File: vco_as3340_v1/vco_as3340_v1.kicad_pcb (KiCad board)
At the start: 2 copper layers, 40 x 100 mm, 88 parts, among them J1 Conn_02x05_Odd_Even, J2 FREQ_CV, J3 SOFT_SYNC, J4 TRIANGLE, J5 SAWTOOTH, J6 PULSE, U1 LM7805_TO220, U2 L7905, U3 AS3340, U4 TL072, U5 TL072, U6 TL072, U7 TL072

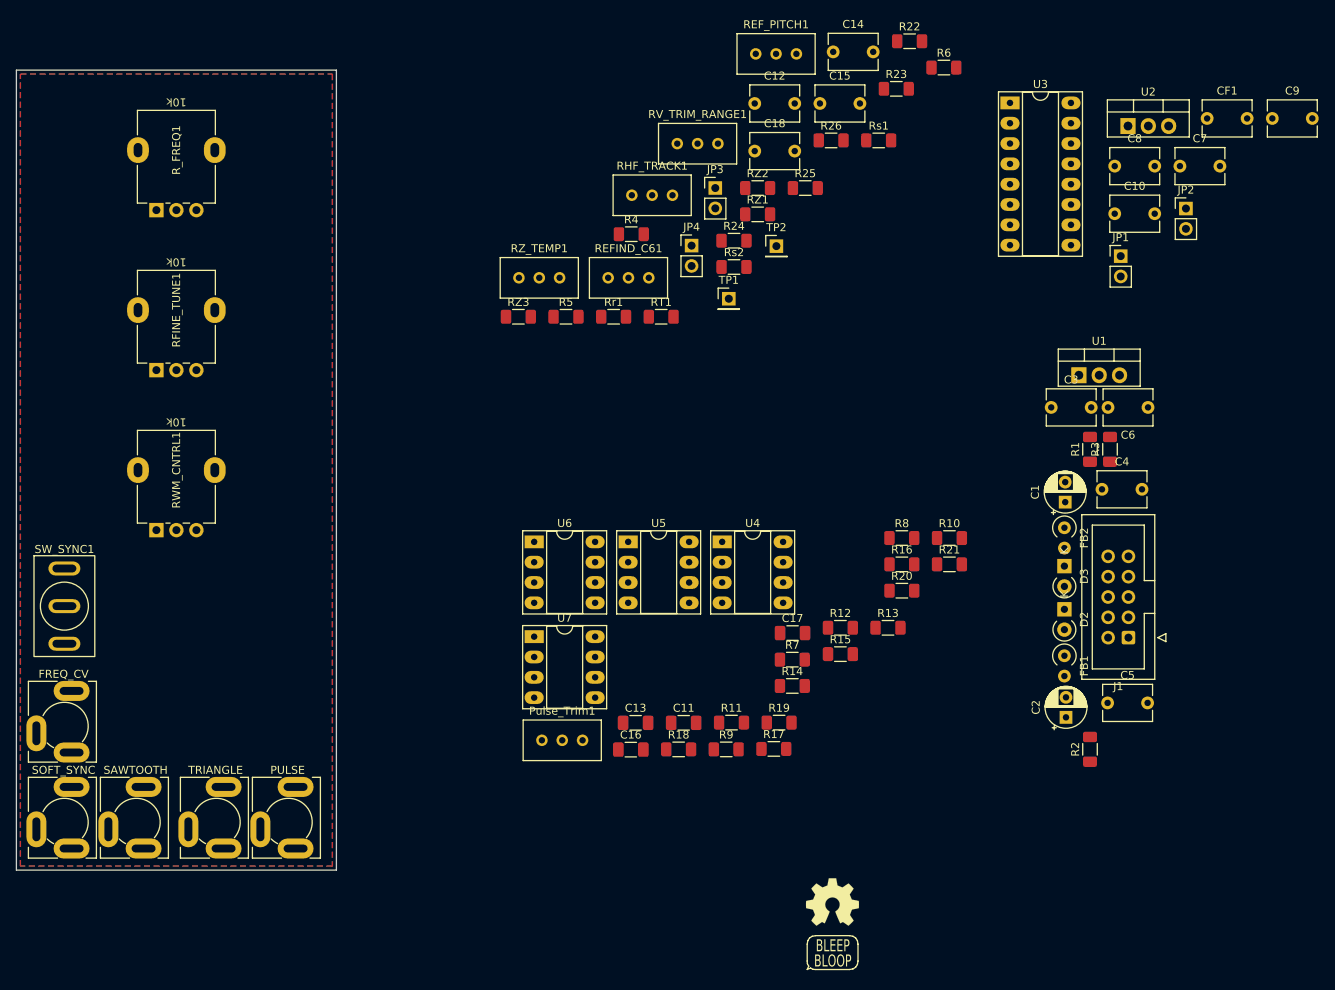
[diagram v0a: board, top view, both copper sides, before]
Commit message: Schematic update from breadboarding, start layout
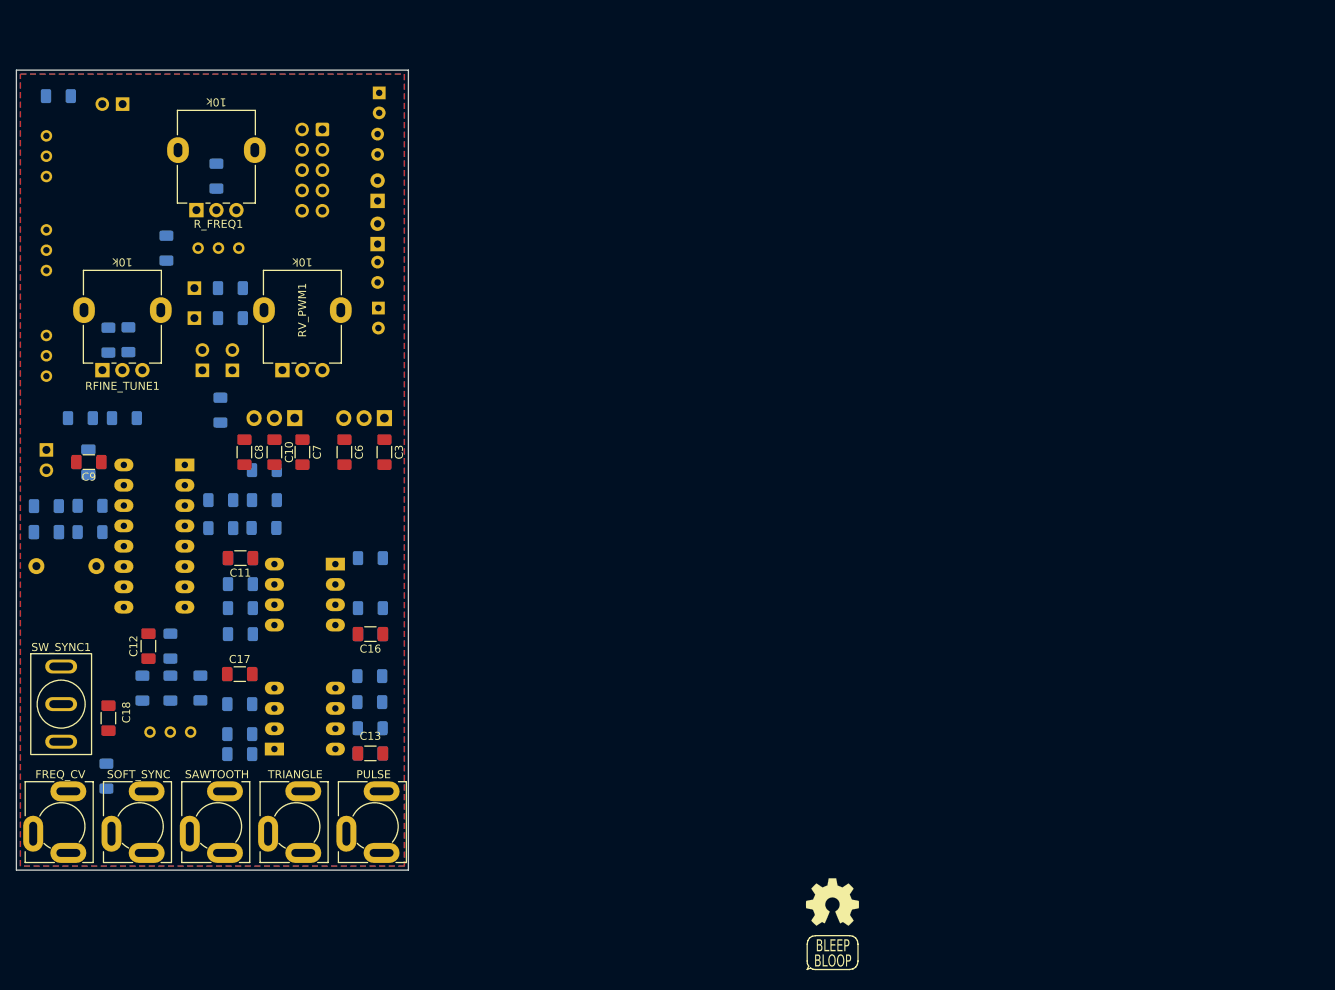
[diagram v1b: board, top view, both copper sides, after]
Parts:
- removed C4, C5: 10nF, Capacitor_THT:C_Disc_D6.0mm_W4.4mm_P5.00mm
- removed Pulse_Trim1: 100k, Potentiometer_THT:Potentiometer_Bourns_3296W_Vertical
- removed RV_TRIM_RANGE1: 1k, Potentiometer_THT:Potentiometer_Bourns_3296W_Vertical
- removed RWM_CNTRL1: 10k, My Stuff:Potentiometer_Alpha_RD901F-40-00D_Single_Vertical_w_3d
- removed RZ3: 18k, Resistor_SMD:R_1206_3216Metric_Pad1.30x1.75mm_HandSolder
- removed U6, U7: TL072, Package_DIP:DIP-8_W7.62mm_Socket_LongPads
- added R27: 15k, Resistor_SMD:R_1206_3216Metric_Pad1.30x1.75mm_HandSolder, B.Cu at (184.2, 111.0)
- added R28: 15k, Resistor_SMD:R_1206_3216Metric_Pad1.30x1.75mm_HandSolder, B.Cu at (168.0, 111.0)
- added R29: 100k, Resistor_SMD:R_1206_3216Metric_Pad1.30x1.75mm_HandSolder, B.Cu at (167.9, 129.2)
- added R30: 100k, Resistor_SMD:R_1206_3216Metric_Pad1.30x1.75mm_HandSolder, B.Cu at (167.9, 133.0)
- added RV_PWM1: 10k, My Stuff:Potentiometer_Alpha_RD901F-40-00D_Single_Vertical_w_3d, F.Cu at (175.8, 80.0)
- added RV_SCALE_ADJ1: 1k, Potentiometer_THT:Potentiometer_Bourns_3296W_Vertical, B.Cu at (143.8, 75.0)
- added Rr2: 330k, Resistor_SMD:R_1206_3216Metric_Pad1.30x1.75mm_HandSolder, B.Cu at (153.5, 93.5)
- C1, C2, D2, D3, FB1, FB2, J1, JP1, JP2, JP3, JP4, R1, R11, R12, R13, R14, R15, R16, R17, R18, R19, R20, R21, R23, R24, R25, R26, R3, R4, R5, R6, R7, R8, REFIND_C61, REF_PITCH1, RHF_TRACK1, RT1, RZ1, RZ_TEMP1, TP1, TP2, U1, U2, U3, U4, U5: moved to B.Cu
- C10, C12, C18, C3, C6, C7, C8, C9: footprint Capacitor_THT:C_Disc_D6.0mm_W4.4mm_P5.00mm -> Capacitor_SMD:C_1206_3216Metric_Pad1.33x1.80mm_HandSolder
- C14, C15: footprint Capacitor_THT:C_Disc_D6.0mm_W4.4mm_P5.00mm -> Capacitor_SMD:C_1206_3216Metric_Pad1.33x1.80mm_HandSolder; moved to B.Cu
- CF1: footprint Capacitor_THT:C_Disc_D6.0mm_W4.4mm_P5.00mm -> Capacitor_THT:C_Rect_L10.0mm_W2.5mm_P7.50mm_MKS4; moved to B.Cu
- R10: value 100k -> 200k; moved to B.Cu
- R2: value 220k -> 150k; moved to B.Cu
- R22: value 470 -> 1M; moved to B.Cu
- R9: value 100k -> 120k; moved to B.Cu
- RZ2: value 18k -> 13k; moved to B.Cu
- Rr1: value 1.8M -> 1M; moved to B.Cu
- Rs1: value 1.62k -> 1k; moved to B.Cu
- Rs2: value 1.5k -> 620; moved to B.Cu
- moved C9 154.0 mm to (149.1, 99.0), turned to 180 degrees
- moved R2 152.6 mm to (145.2, 53.2), turned to 0 degrees
- moved CF1 149.7 mm to (150.0, 112.0), turned to 180 degrees
- moved R3 131.9 mm to (151.2, 138.2), turned to -90 degrees
- moved R22 122.8 mm to (159.2, 127.2), turned to -90 degrees
- moved JP2 120.9 mm to (167.0, 87.5)
- moved J1 119.1 mm to (178.3, 57.4)
- moved C2 116.0 mm to (185.4, 52.8), turned to -90 degrees
- moved JP1 115.7 mm to (163.2, 87.5)
- moved C7 115.4 mm to (175.8, 97.8), turned to -90 degrees
- moved C14 115.2 mm to (143.8, 107.8), turned to 180 degrees
- moved C8 114.5 mm to (168.5, 97.8), turned to -90 degrees
- moved U3 112.6 mm to (161.1, 99.3), turned to 180 degrees
- moved U2 110.4 mm to (174.8, 93.5), turned to 180 degrees
- moved R6 109.9 mm to (151.5, 83.8), turned to 90 degrees
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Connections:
- C15 pad 1: Net-(RV_TRIM_RANGE1-Pad2) -> GND
- J2 pad R: (no net) -> unconnected-(J2-PadR)
- J3 pad R: (no net) -> unconnected-(J3-PadR)
- J4 pad R: (no net) -> unconnected-(J4-PadR)
- J5 pad R: (no net) -> unconnected-(J5-PadR)
- J6 pad R: (no net) -> unconnected-(J6-PadR)
- R14 pad 1: Net-(R13-Pad2) -> Net-(R14-Pad1)
- R15 pad 2: Net-(R11-Pad1) -> Net-(R15-Pad2)
- RZ2 pad 1: Net-(RZ2-Pad1) -> /Inputs/Scale Adjust 1
- Rr1 pad 1: /Inputs/Linear FM -> Net-(Rr1-Pad1)
- Rs1 pad 2: Net-(RV_TRIM_RANGE1-Pad1) -> Net-(Rs1-Pad2)
- Rs2 pad 1: Net-(RV_TRIM_RANGE1-Pad3) -> Net-(Rs1-Pad2)
- Rs2 pad 2: GND -> Net-(RV_SCALE_ADJ1-Pad1)
- U4 pad 1: Net-(R13-Pad2) -> Net-(R14-Pad1)
- U4 pad 4: (no net) -> -12V
- U4 pad 5: /Outputs/Triangle Output -> GND
- U4 pad 6: Net-(R10-Pad1) -> Net-(R14-Pad2)
- U4 pad 7: Net-(R10-Pad2) -> Net-(R11-Pad1)
- U4 pad 8: (no net) -> +12V
- U5 pad 4: (no net) -> -12V
- U5 pad 5: GND -> /Outputs/Triangle Output
- U5 pad 6: Net-(R14-Pad2) -> Net-(R10-Pad1)
- U5 pad 7: Net-(R11-Pad1) -> Net-(R10-Pad2)
- U5 pad 8: (no net) -> +12V
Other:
- board size 40 x 100 mm -> 49 x 100 mm
- board text added: "50.8mm = 10HP"
- board text removed: "15.24 = 3HP"

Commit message: Layout and routing done
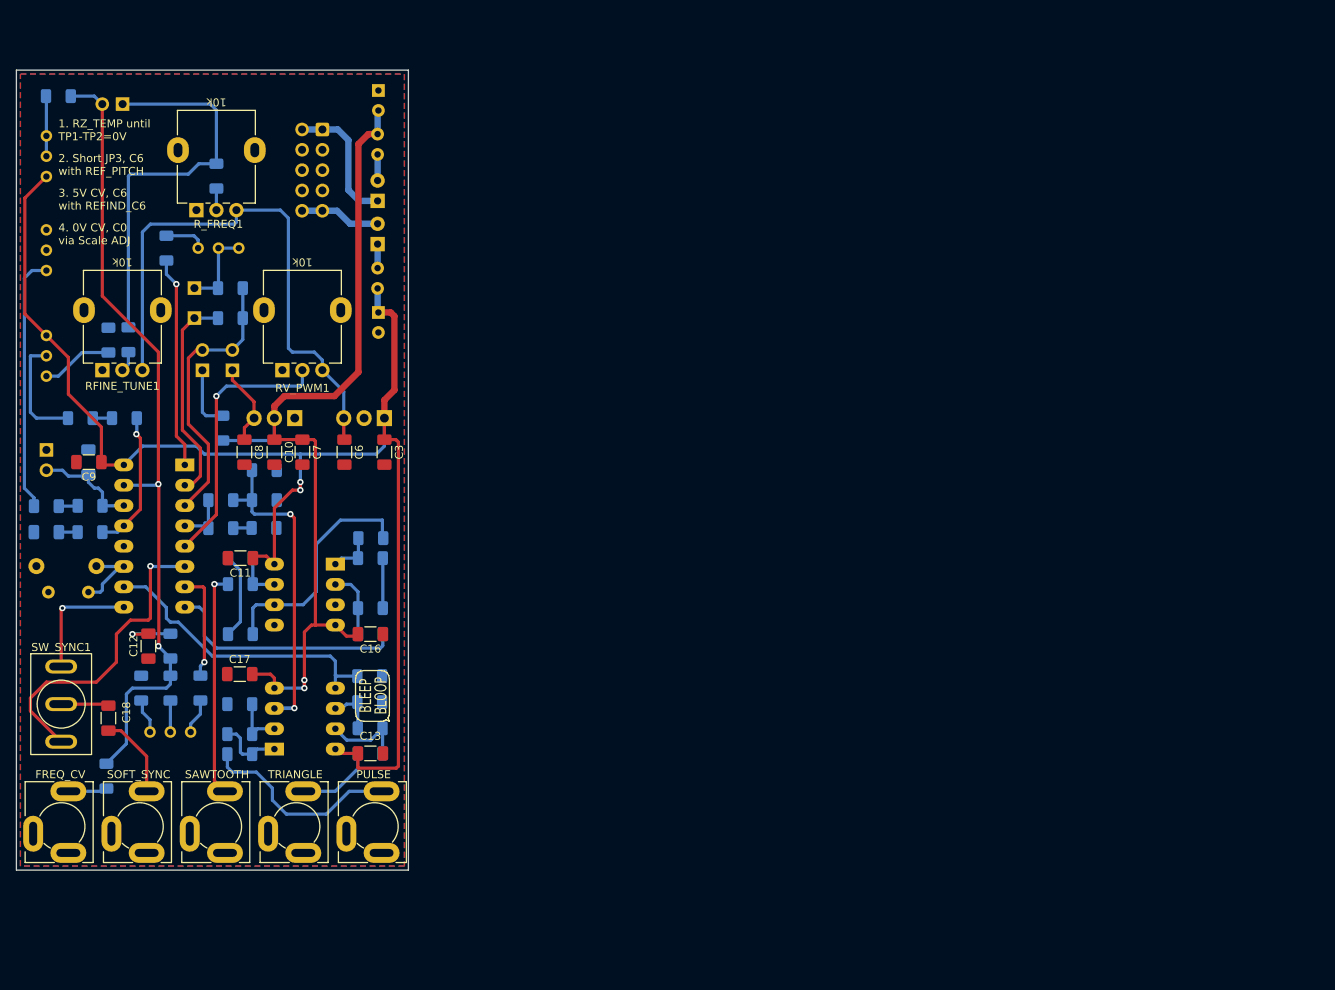
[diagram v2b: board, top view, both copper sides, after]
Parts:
- added CF2: 1nF, Capacitor_THT:C_Rect_L7.0mm_W2.5mm_P5.00mm, B.Cu at (149.0, 115.2)
- LOGO3: moved to B.Cu
- moved LOGO2 98.3 mm to (151.2, 122.8), turned to 90 degrees
- moved LOGO3 78.1 mm to (184.0, 101.8), turned to 180 degrees
- moved LOGO1 65.8 mm to (184.5, 128.2), turned to 90 degrees
- moved R14 18.5 mm to (184.3, 108.5)
- moved R1 2.26 mm to (165.8, 94.8)
- moved FB2 1.79 mm to (185.2, 74.8), turned to -90 degrees
- moved C1 0.55 mm to (185.2, 80.3)
- moved C2 0.32 mm to (185.2, 52.5)
- moved R24 0.15 mm to (155.6, 127.2)
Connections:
- RFINE_TUNE1 pad MP: (no net) -> GND
- RV_PWM1 pad MP: (no net) -> GND
- R_FREQ1 pad MP: (no net) -> GND
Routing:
- net +12V: track 0.00 -> 175.1 mm, vias 0 -> 2
- net -12V: track 0.00 -> 111.7 mm, vias 0 -> 2
- net /Inputs/Frequency Control: track 0.00 -> 100.5 mm, vias 0 -> 2
- net +5V: track 0.00 -> 70.1 mm
- net Net-(JP4-Pad1): track 0.00 -> 49.3 mm
- net Net-(R16-Pad1): track 0.00 -> 41.7 mm, vias 0 -> 2
- net /Inputs/Hard Sync: track 0.00 -> 39.1 mm, vias 0 -> 1
- net /Outputs/Triangle Output: track 0.00 -> 37.2 mm
- net VEE: track 0.00 -> 34.9 mm
- net /Inputs/PWM Control: track 0.00 -> 33.5 mm, vias 0 -> 1
- net Net-(RV_SCALE_ADJ1-Pad1): track 0.00 -> 32.1 mm
- net /Outputs/Sawtooth Output: track 0.00 -> 30.2 mm
- net Net-(R14-Pad2): track 0.00 -> 29.8 mm
- net Net-(J5-PadT): track 0.00 -> 28.1 mm, vias 0 -> 1
- net /Inputs/Scale Adjust 2: track 0.00 -> 26.7 mm
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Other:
- board text added: "1. RZ_TEMP until TP1-TP2=0V"
- board text added: "100k"
- board text added: "10k"
- board text added: "1k"
- board text added: "2. Short JP3, C6 with REF_PITCH"
- board text added: "3. 5V CV, C6 with REFIND_C6"
- board text added: "4. 0V CV, C0 via Scale ADJ"
- board text added: "AS3340"
- board text added: "AS3340 VCO"
- board text added: "LM7805"
- board text added: "LM7905"
- board text added: "RobotDialogs"
- board text added: "TL072"
- board text added: "v1.0 July 2022"

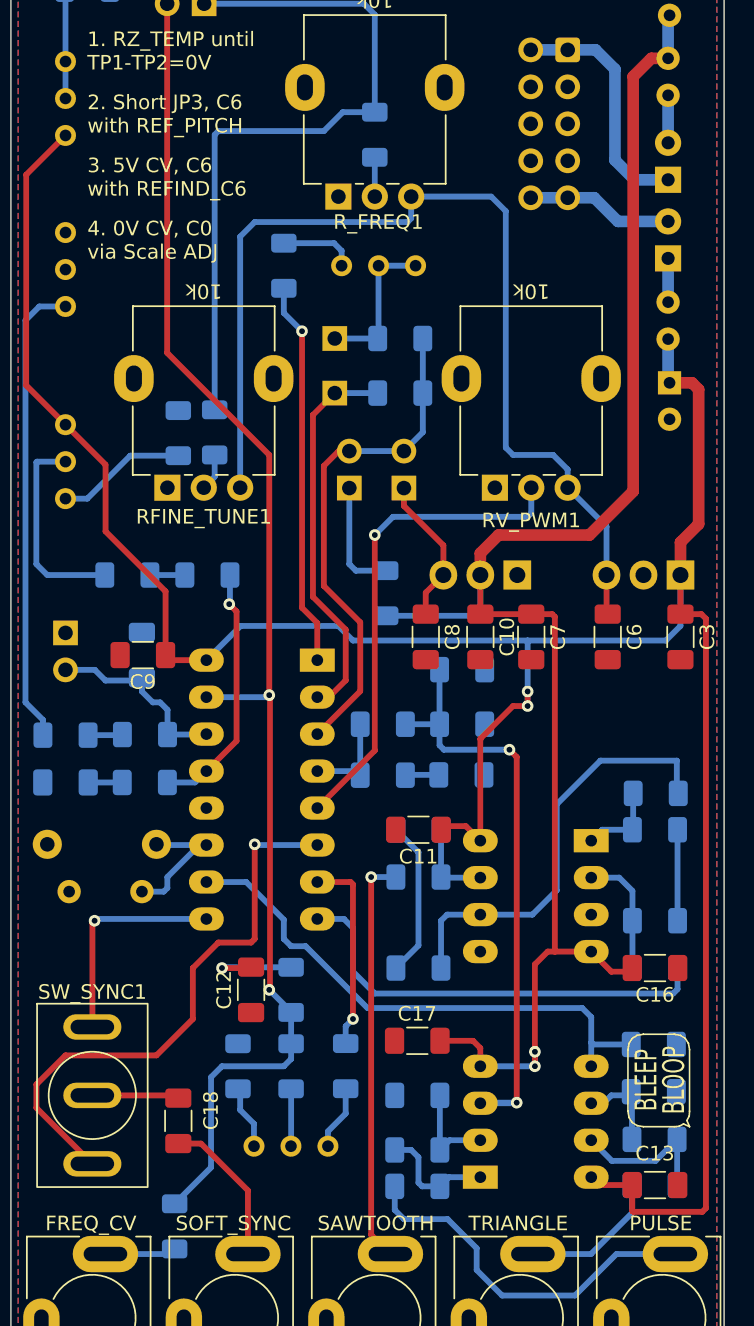
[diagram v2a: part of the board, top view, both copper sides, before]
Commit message: Geographic re-annotate and cleanup
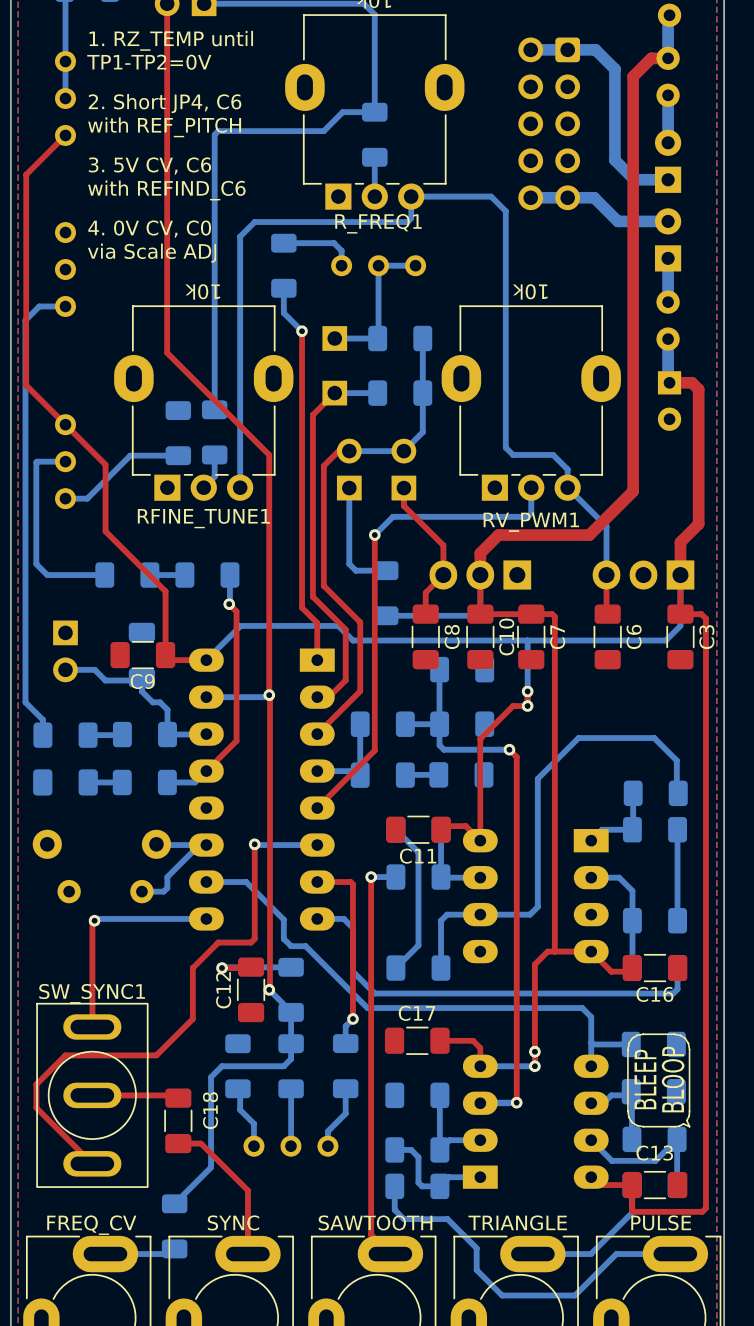
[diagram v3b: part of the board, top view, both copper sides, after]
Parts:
- J101: renamed from J3; value SOFT_SYNC -> SYNC
- renumbered C1 to C4, C15 to C5, D2 to D1, D3 to D2, RHF_TRACK1 to HF_TRACK1, J2 to J100, J5 to J102, J4 to J103, J6 to J104, J1 to J2, JP4 to JP1, JP1 to JP3, JP3 to JP4, LOGO2 to LOGO101, LOGO3 to LOGO2, R2 to R1, R17 to R10, R14 to R11, R5 to R12, R27 to R13, R28 to R14, R11 to R15, R13 to R16, R12 to R17, R15 to R18, R4 to R19, R23 to R2, R8 to R20, R25 to R21, R24 to R23, R9 to R24, R29 to R25, R10 to R26, R30 to R27, R7 to R28, R18 to R29, R26 to R3, R3 to R30, R6 to R4, R1 to R5, R21 to R6, R20 to R7, R16 to R8, R19 to R9, REFIND_C61 to REFIND_C6, RZ2 to RZ1, RZ1 to RZ2, Rr2 to Rr1, Rr1 to Rr2, RV_SCALE_ADJ1 to SCALE_ADJ1, TP2 to TP1, TP1 to TP2
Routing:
- net Net-(R11-Pad2): track 29.8 -> 32.7 mm
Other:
- board text added: "2. Short JP4, C6 with REF_PITCH"
- board text added: "FREQ"
- board text added: "PULSE"
- board text added: "SAWTOOTH"
- board text added: "SYNC"
- board text added: "TRIANGLE"
- board text removed: "2. Short JP3, C6 with REF_PITCH"
